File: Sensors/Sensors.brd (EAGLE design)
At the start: 101.6 x 53.3 mm, 45 parts, among them IC1 MAX31855, IC2 MAX31855, IC3 MAX31855

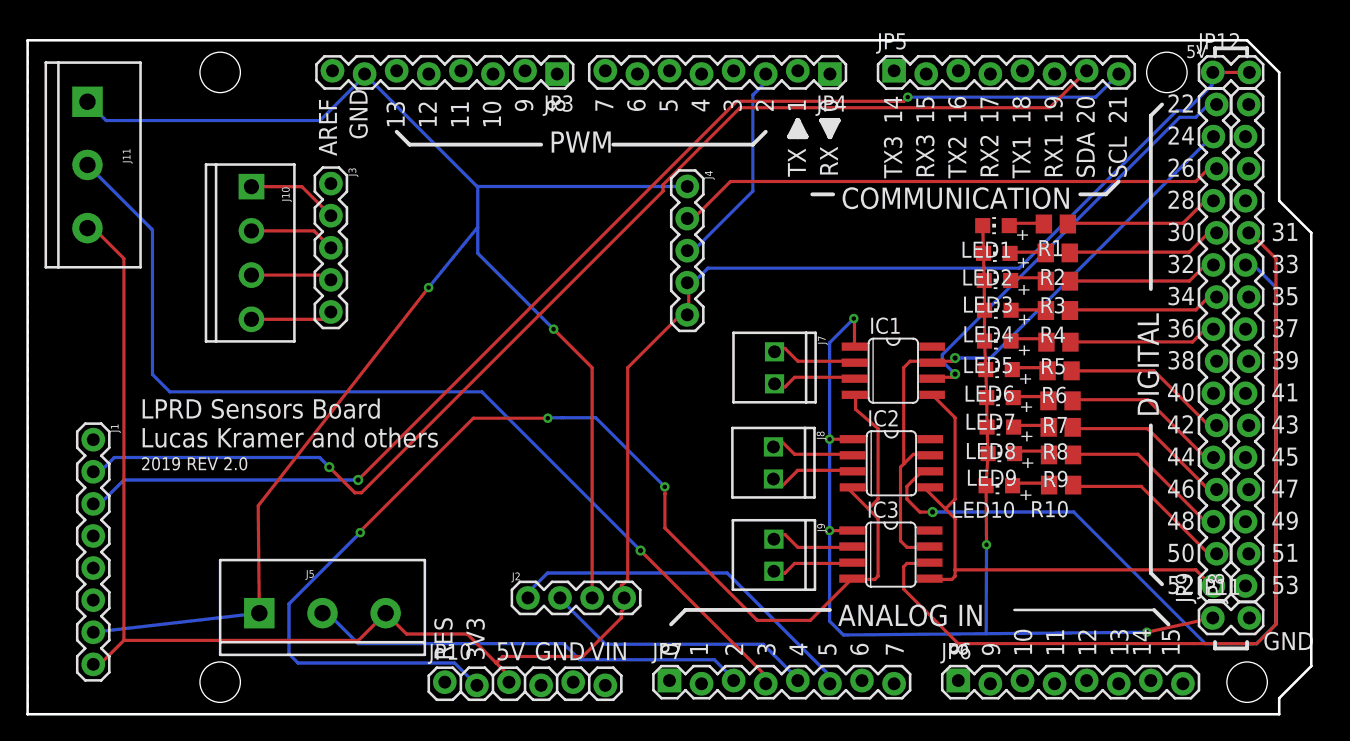
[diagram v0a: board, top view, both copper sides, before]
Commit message: Removed thermocouples, added JSTs
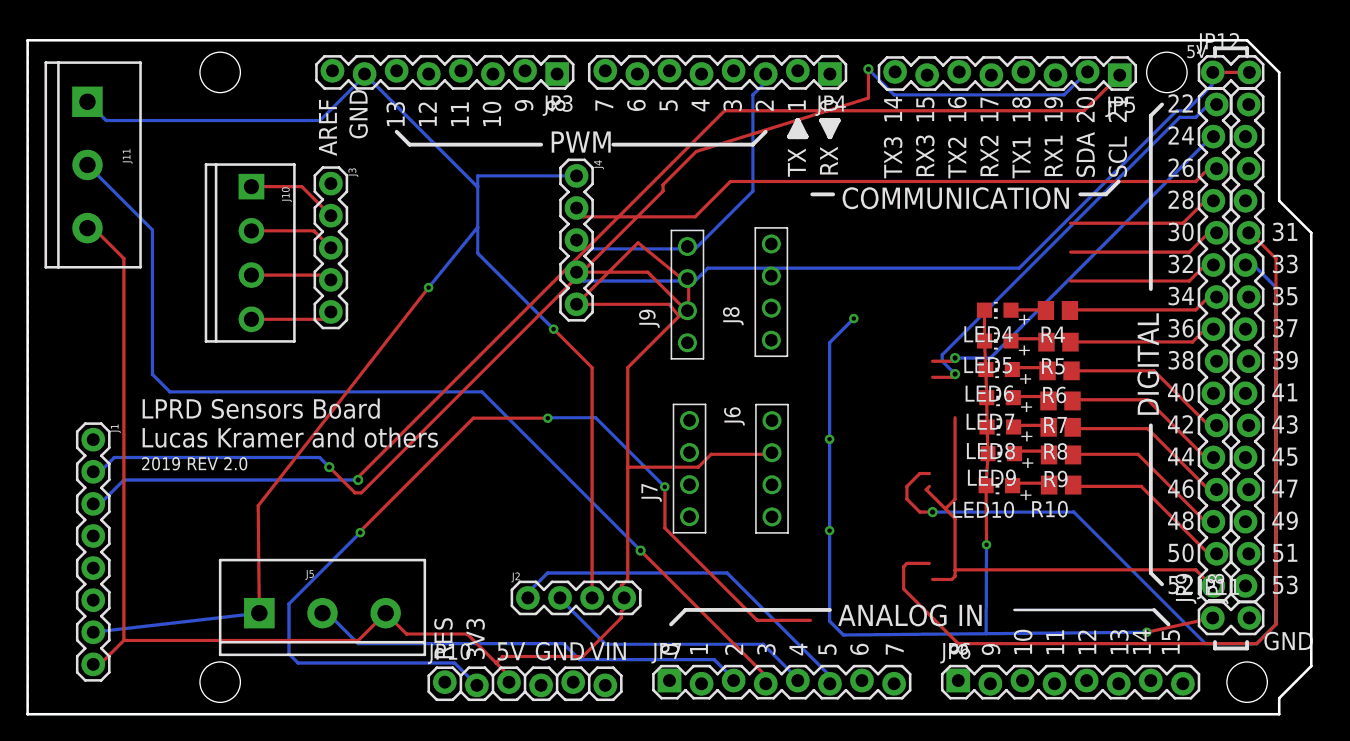
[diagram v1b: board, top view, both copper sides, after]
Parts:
- removed IC1, IC2, IC3: MAX31855, adafruit:SO08
- removed LED1, LED2, LED3: (no value), adafruit:CHIP-LED0805
- removed R1, R2, R3: 1000, resistor:R0805
- added J6: JST_CONNECTOR, LPRD_RELAY:B4B-XH-A(LF)(SN)
- J7, J8, J9: value (none) -> JST_CONNECTOR; device SparkFun-Connectors:1X02_2.54_SCREWTERM -> LPRD_RELAY:B4B-XH-A(LF)(SN)
- moved J9 21.7 mm to (52.2, 34.5), turned to 90 degrees
- moved JP5 17.9 mm to (86.4, 50.7), turned to 180 degrees
- moved J8 13.5 mm to (58.9, 34.7), turned to 90 degrees
- moved J7 10.4 mm to (52.4, 20.7), turned to 90 degrees
- moved J4 8.80 mm to (43.4, 42.6)
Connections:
- removed net D20: JP5.2
- removed net D21: JP5.1
- removed net N$1: LED1.A, R1.2
- removed net N$10: IC1.3, J7.P1
- removed net N$11: IC2.2, J8.P2
- removed net N$12: IC2.3, J8.P1
- removed net N$13: IC3.2, J9.P2
- removed net N$14: IC3.3, J9.P1
- removed net N$2: LED2.A, R2.2
- removed net N$3: LED3.A, R3.2
- removed net N$8: IC1.2, J7.P2
- new net VOUT_TERMPERATURE_1: J6.P$4
- net 3.3V: no longer IC1.4, IC2.4, IC3.4
- net 5V: now also J6.P$3, J7.P$3, J8.P$4, J9.P$4
- net GND: now also J6.P$2, J7.P$2, J8.P$2, J9.P$2; no longer IC1.1, IC2.1, IC3.1, LED1.C, LED2.C, LED3.C
- net MAXCLK: no longer IC1.5, IC2.5, IC3.5
- net MAXCS1: no longer IC1.6
- net MAXCS2: no longer IC2.6
- net MAXCS3: no longer IC3.6
- net MAXDO: no longer IC1.7, IC2.7, IC3.7
- net SCL: now also JP5.1; no longer JP5.8
- net SDA: now also JP5.2; no longer JP5.7
- net THERMO1_LED: no longer R1.1
- net THERMO2_LED: no longer R2.1
- net THERMO3_LED: no longer R3.1
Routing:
- net 5V: track 163.9 -> 214.6 mm
- net 3.3V: track 101.1 -> 75.8 mm
- net MAXDO: track 51.0 -> 29.6 mm
- net GND: track 233.4 -> 213.1 mm
- net FORCE_CLK: track 43.5 -> 52.6 mm
- net FORCE_DAT: track 16.8 -> 25.9 mm
- net N$12: track 7.08 -> 0.00 mm
- net N$11: track 6.93 -> 0.00 mm
- net N$8: track 6.89 -> 0.00 mm
- net N$10: track 6.86 -> 0.00 mm
- net N$13: track 6.77 -> 0.00 mm
- net N$14: track 6.58 -> 0.00 mm
- net MAXCLK: track 41.6 -> 38.5 mm
- net N$3: track 3.00 -> 0.00 mm
- net N$1: track 2.91 -> 0.00 mm
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
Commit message: Updated Schematic, pins now aligned and connected
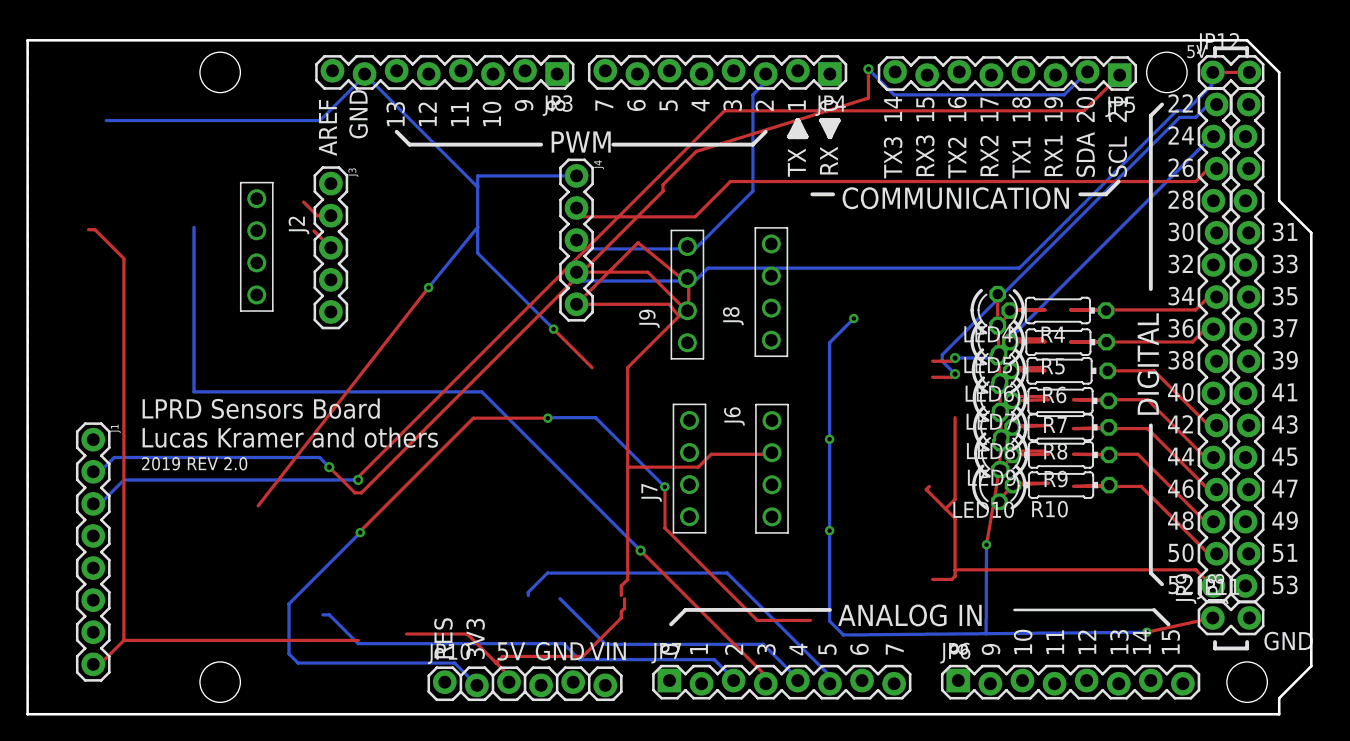
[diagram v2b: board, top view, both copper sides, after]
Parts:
- removed J10: (no value), SparkFun-Connectors:SCREWTERMINAL-3.5MM-4
- removed J11, J5: (no value), SparkFun-Connectors:SCREWTERMINAL-5MM-3
- J2: value (none) -> JST_CONNECTOR; device SparkFun-Connectors:1X04 -> LPRD_RELAY:B4B-XH-A(LF)(SN)
- LED10, LED4, LED5, LED6, LED7, LED8, LED9: device adafruit:CHIP-LED0805 -> led:LED3MM
- R10, R4, R5, R6, R7, R8, R9: device resistor:R0805 -> rcl:0204/7
- moved J2 34.1 mm to (18.1, 35.7), turned to 270 degrees
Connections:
- net MAXCS2 renamed D33
- net MAXCS3 renamed D31
- net THERMO1_LED renamed D46
- net THERMO2_LED renamed D44
- net THERMO3_LED renamed D42
- removed net VOUT_TERMPERATURE_1: J6.P$4
- net 5V: now also J8.P$3, J9.P$3; no longer J11.3, J2.4, J5.3, J8.P$4, J9.P$4
- net A+/GREEN: now also J2.P$1; no longer J10.1
- net A-/WHITE: now also J2.P$2; no longer J10.2
- net E+/RED: now also J2.P$4; no longer J10.4
- net E-/BLACK: now also J2.P$3; no longer J10.3
- net GND: now also J6.P$4, J7.P$4, J8.P$4, J9.P$4, LED10.K, LED4.K, LED5.K, LED6.K, LED7.K, LED8.K, LED9.K; no longer J11.1, J2.3, J5.1, J6.P$2, J7.P$2, J8.P$2, J9.P$2, LED10.C, LED4.C, LED5.C, LED6.C, LED7.C, LED8.C, LED9.C
- net VOUT_PRESSURE_1: now also J8.P$2; no longer J5.2
- net VOUT_PRESSURE_2: now also J9.P$2; no longer J11.2
- net VOUT_TEMPERATURE_1: now also J6.P$2; no longer J2.2
- net VOUT_TEMPERATURE_2: now also J7.P$2; no longer J2.1
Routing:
- net D33: track 68.1 -> 0.00 mm, vias 1 -> 0
- net D31: track 67.8 -> 0.00 mm
- net GND: track 213.1 -> 172.4 mm
- net D44: track 12.2 -> 0.00 mm
- net D46: track 12.0 -> 0.00 mm
- net D42: track 11.8 -> 0.00 mm
- net VOUT_PRESSURE_2: track 77.8 -> 68.2 mm
- net E-/BLACK: track 6.44 -> 0.54 mm
- net 5V: track 214.6 -> 208.7 mm
- net E+/RED: track 6.53 -> 0.82 mm
- net A-/WHITE: track 6.84 -> 1.89 mm
- net A+/GREEN: track 7.24 -> 2.61 mm
- net N$7: track 2.98 -> 7.34 mm
- net N$16: track 2.96 -> 7.32 mm
- net N$15: track 2.93 -> 7.23 mm
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
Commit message: Rewired force JST mount
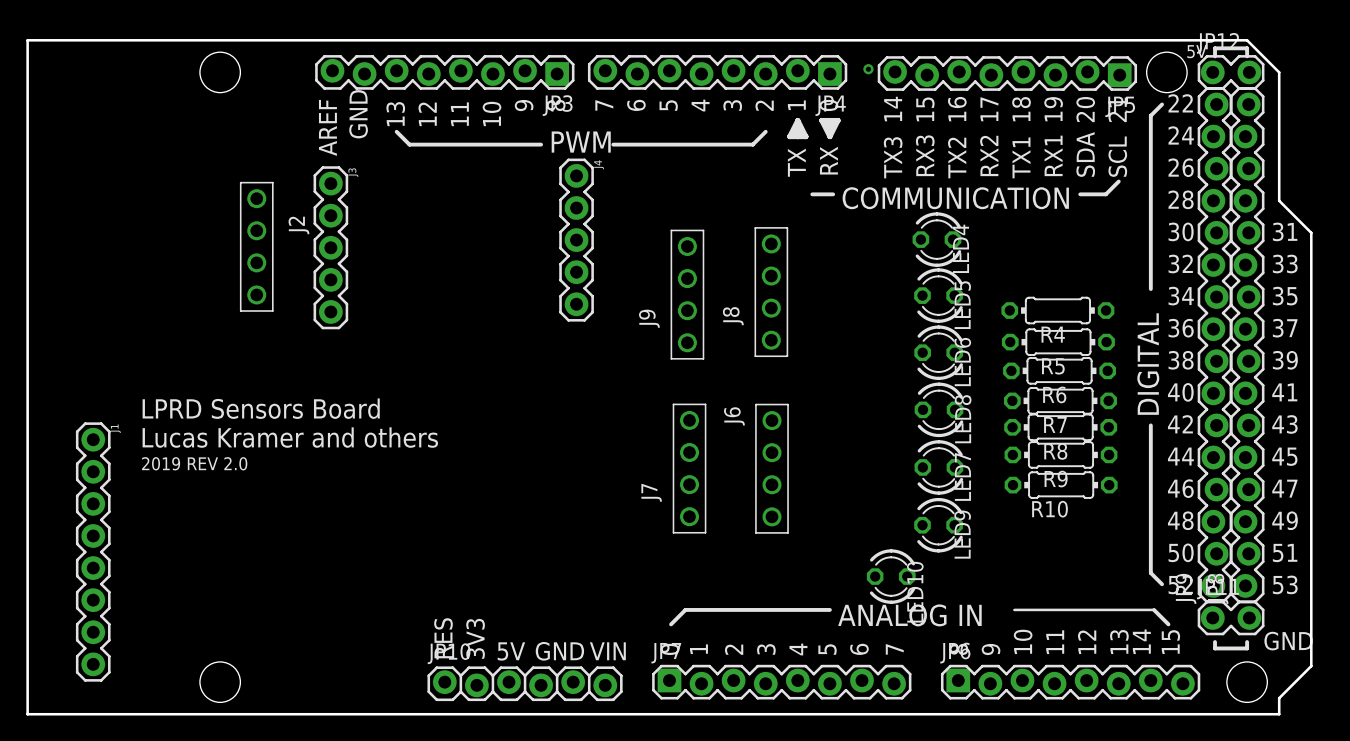
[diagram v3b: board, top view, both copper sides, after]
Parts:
- moved LED10 11.2 mm to (68.4, 10.9), turned to 180 degrees
- moved LED9 7.53 mm to (72.1, 15.0), turned to 180 degrees
- moved LED4 7.38 mm to (72.0, 37.6), turned to 180 degrees
- moved LED7 7.34 mm to (72.1, 19.5), turned to 180 degrees
- moved LED5 5.91 mm to (72.1, 33.1), turned to 180 degrees
- moved LED8 5.04 mm to (72.1, 24.1), turned to 180 degrees
- moved LED6 4.96 mm to (72.1, 28.6), turned to 180 degrees
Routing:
- net 5V: track 208.7 -> 0.00 mm
- net GND: track 172.4 -> 0.15 mm, vias 7 -> 0
- net SDA: track 96.3 -> 0.00 mm, vias 2 -> 1
- net SCL: track 95.4 -> 0.00 mm, vias 1 -> 0
- net 3.3V: track 75.8 -> 0.00 mm, vias 3 -> 0
- net VOUT_PRESSURE_2: track 68.2 -> 0.00 mm, vias 1 -> 0
- net FORCE_CLK: track 52.6 -> 0.00 mm
- net MAXCLK: track 38.5 -> 0.00 mm
- net VOUT_PRESSURE_1: track 34.7 -> 0.00 mm
- net MAXCS1: track 33.8 -> 0.00 mm, vias 1 -> 0
- net MAXDO: track 29.6 -> 0.00 mm, vias 1 -> 0
- net VOUT_TEMPERATURE_2: track 28.8 -> 0.00 mm
- net FORCE_DAT: track 25.9 -> 0.00 mm
- net VOUT_TEMPERATURE_1: track 21.6 -> 0.00 mm
- net PRESSURE2_LED: track 16.3 -> 0.00 mm
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
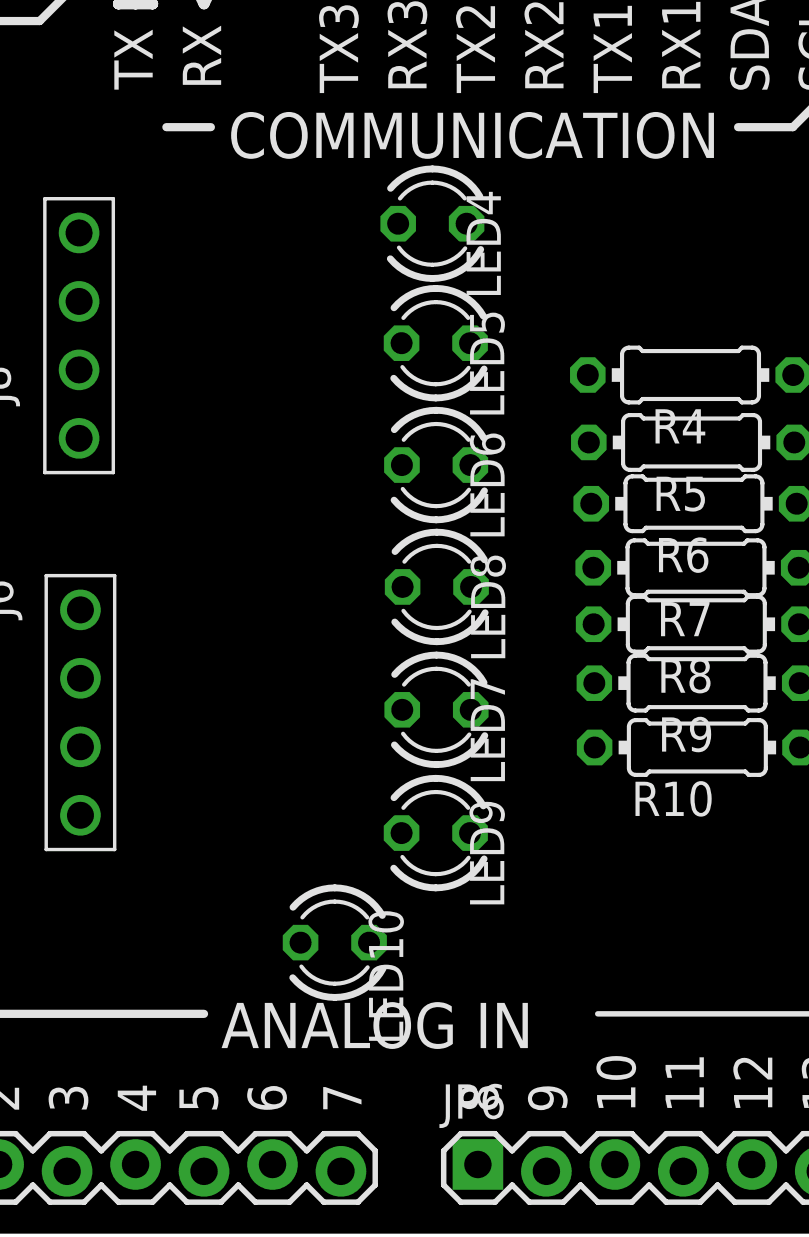
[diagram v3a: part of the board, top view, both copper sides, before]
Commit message: Refixed names on load cell JST
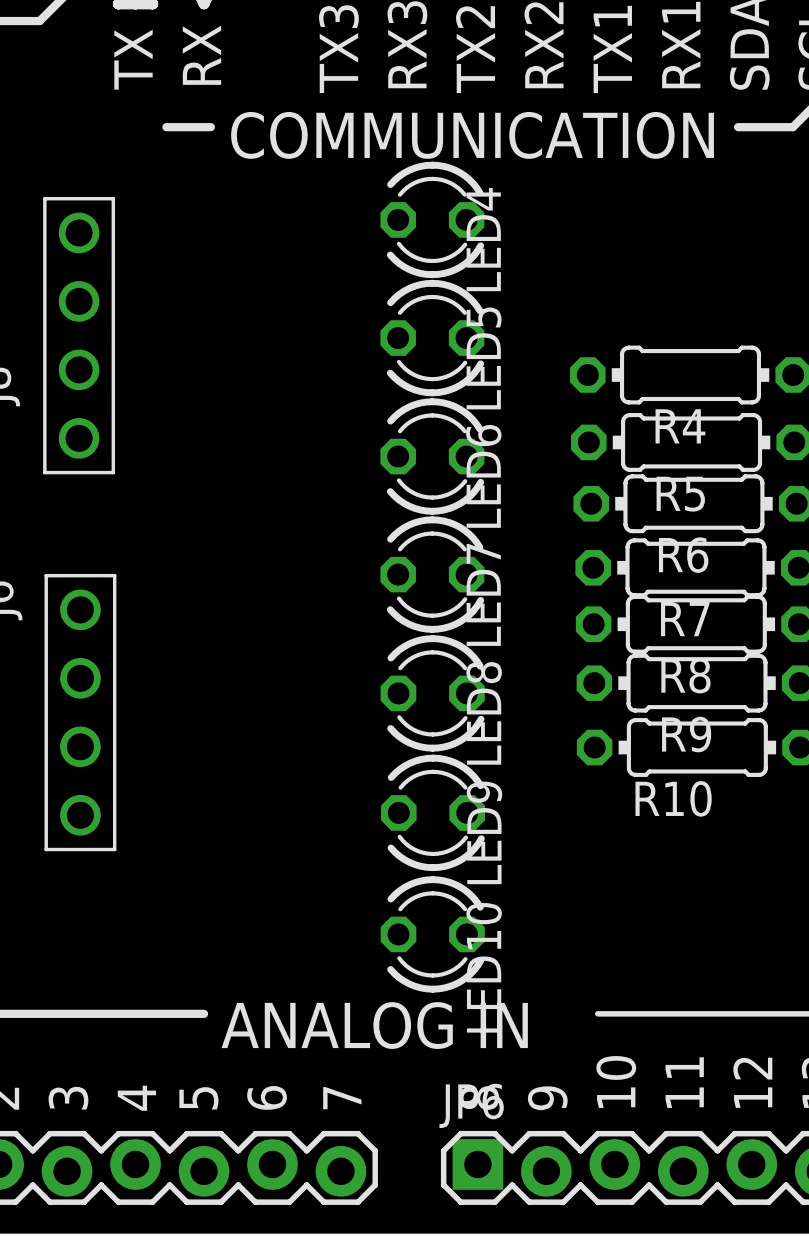
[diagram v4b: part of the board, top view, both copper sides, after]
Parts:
- moved LED7 5.02 mm to (72.0, 24.5)
- moved LED8 3.95 mm to (72.0, 20.1)
- moved LED10 3.64 mm to (72.0, 11.2)
- moved LED9 0.76 mm to (72.0, 15.7)
- moved LED6 0.35 mm to (72.0, 28.9)
- moved LED5 0.23 mm to (72.0, 33.3)
- moved LED4 0.14 mm to (72.0, 37.7)
